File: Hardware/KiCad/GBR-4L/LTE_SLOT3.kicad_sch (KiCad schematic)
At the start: 0 parts

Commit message: Add modem and SIM schematics
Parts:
- added C301, C302, C303, C304: 100nF, Capacitor_SMD:C_0603_1608Metric, symbol Device:C
- added C305, C306: 100uF 6.3V low-ESR, Capacitor_SMD:C_1210_3225Metric, symbol Device:C
- added J301: EM7565 M.2 Key B socket, symbol Connector:Bus_M.2_Socket_B
- added J302: MODEM_CONTROL, Connector_PinHeader_2.54mm:PinHeader_1x08_P2.54mm_Vertical, symbol Connector_Generic:Conn_01x08
- added R301: 10k, Resistor_SMD:R_0603_1608Metric, symbol Device:R
- added R302, R303: 100R, Resistor_SMD:R_0603_1608Metric, symbol Device:R
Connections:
- new net +3V3_M3: C301.1, C302.1, C303.1, C304.1, C305.1, C306.1, J301.2 (3.3V), J301.4 (3.3V), J301.70 (3.3V), J301.72 (3.3V), J301.74 (3.3V), J302.1 (Pin_1), R301.1
- new net GND: C301.2, C302.2, C303.2, C304.2, C305.2, C306.2, J301.11 (GND), J301.27 (GND), J301.3 (GND), J301.33 (GND), J301.39 (GND), J301.45 (GND), J301.5 (GND), J301.51 (GND), J301.57 (GND), J301.71 (GND), J301.73 (GND), J302.2 (Pin_2)
- new net M3_FULL_CARD_POWER_OFF#: J301.6 (~{FULL_CARD_POWER_OFF}), J302.4 (Pin_4), R301.2
- new net M3_PWR_EN: J302.3 (Pin_3)
- new net M3_RESET#: J301.67 (~{RESET}), R302.2
- new net M3_RESET_CTRL#: J302.5 (Pin_5), R302.1
- new net M3_SIM_DETECT: J301.66 (SIM_DETECT), J302.8 (Pin_8)
- new net M3_UIM_CLK: J301.32 (UIM-CLK)
- new net M3_UIM_DATA: J301.34 (UIM-DATA)
- new net M3_UIM_PWR: J301.36 (UIM-PWR)
- new net M3_UIM_RESET: J301.30 (UIM-RESET)
- new net M3_WWAN_LED#: J301.10 (GPIO_9/DAS/~{DSS}/~{LED1}), J302.7 (Pin_7)
- new net M3_W_DISABLE#: J301.8 (~{W_DISABLE1}), R303.2
- new net M3_W_DISABLE_CTRL#: J302.6 (Pin_6), R303.1
- new net USB_M3_D+: J301.7 (USB_D+)
- new net USB_M3_D-: J301.9 (USB_D-)
- no-connect marks 0 -> 40
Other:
- note added: "Do not drive module I/O until at least 100 ms after the start of power-up."
- note added: "EM7565 MODEM SLOT 3 — M.2 KEY B 3042"
- note added: "M.2 socket footprint intentionally remains unassigned until the connector height is frozen."
- note added: "Route USB as 90-ohm differential; keep the pair on continuous ground and away from buck switch nodes."
- note added: "USB 2.0 only. PCIe, USB 3.0, secondary SIM, antenna-control and reserved pins are NC."
- title: (none) -> GBR-4L EM7565 slot 3

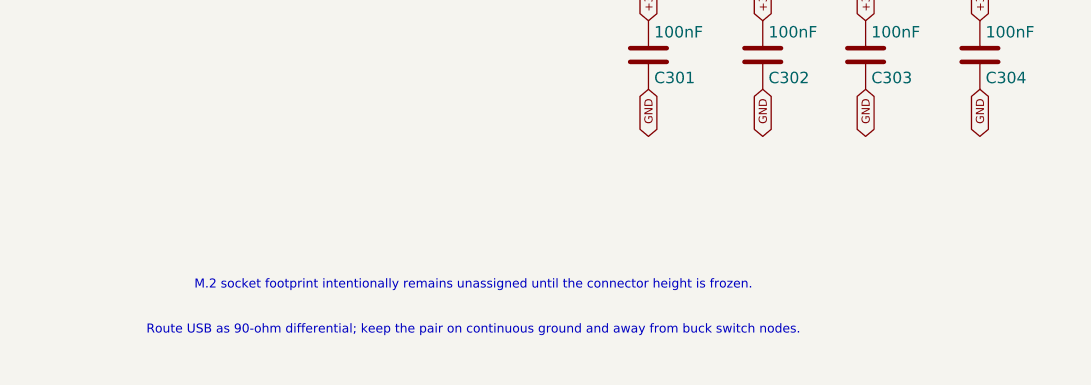
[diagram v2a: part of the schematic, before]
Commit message: Add connector footprints and initial PCB packing
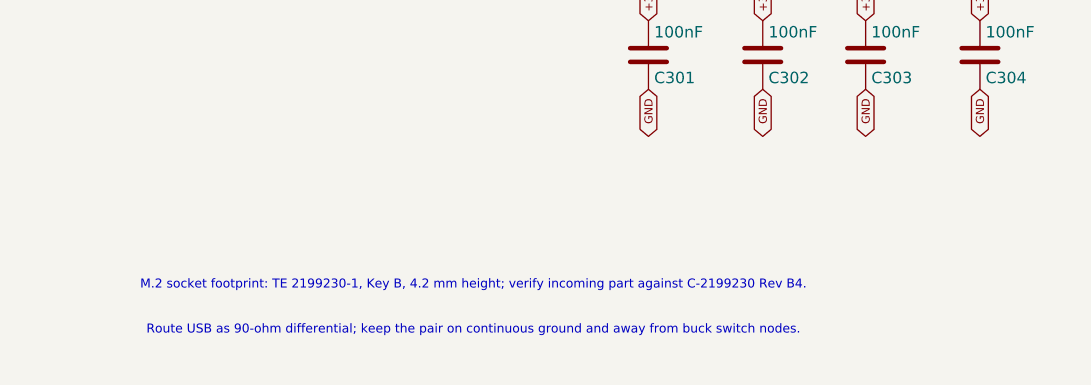
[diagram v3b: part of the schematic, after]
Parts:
- J301: footprint (none) -> GBR-4L:TE_2199230-1_M2_Key-B
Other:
- note added: "M.2 socket footprint: TE 2199230-1, Key B, 4.2 mm height; verify incoming part against C-2199230 Rev B4."
- note removed: "M.2 socket footprint intentionally remains unassigned until the connector height is frozen."
